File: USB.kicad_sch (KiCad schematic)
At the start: 42 parts, among them J3 USB_C_Receptacle_USB2.0, J4 USB_A_Stacked, SW4 SW_DEBUG_MODE, U2 CP2102N-Axx-xQFN24, U3 FSUSB42MUX, U4 FSUSB42MUX, U5 TPD4EUSB30, U6 USB2422, U7 AP2171W, U8 TPD4EUSB30, Y1 24MHz

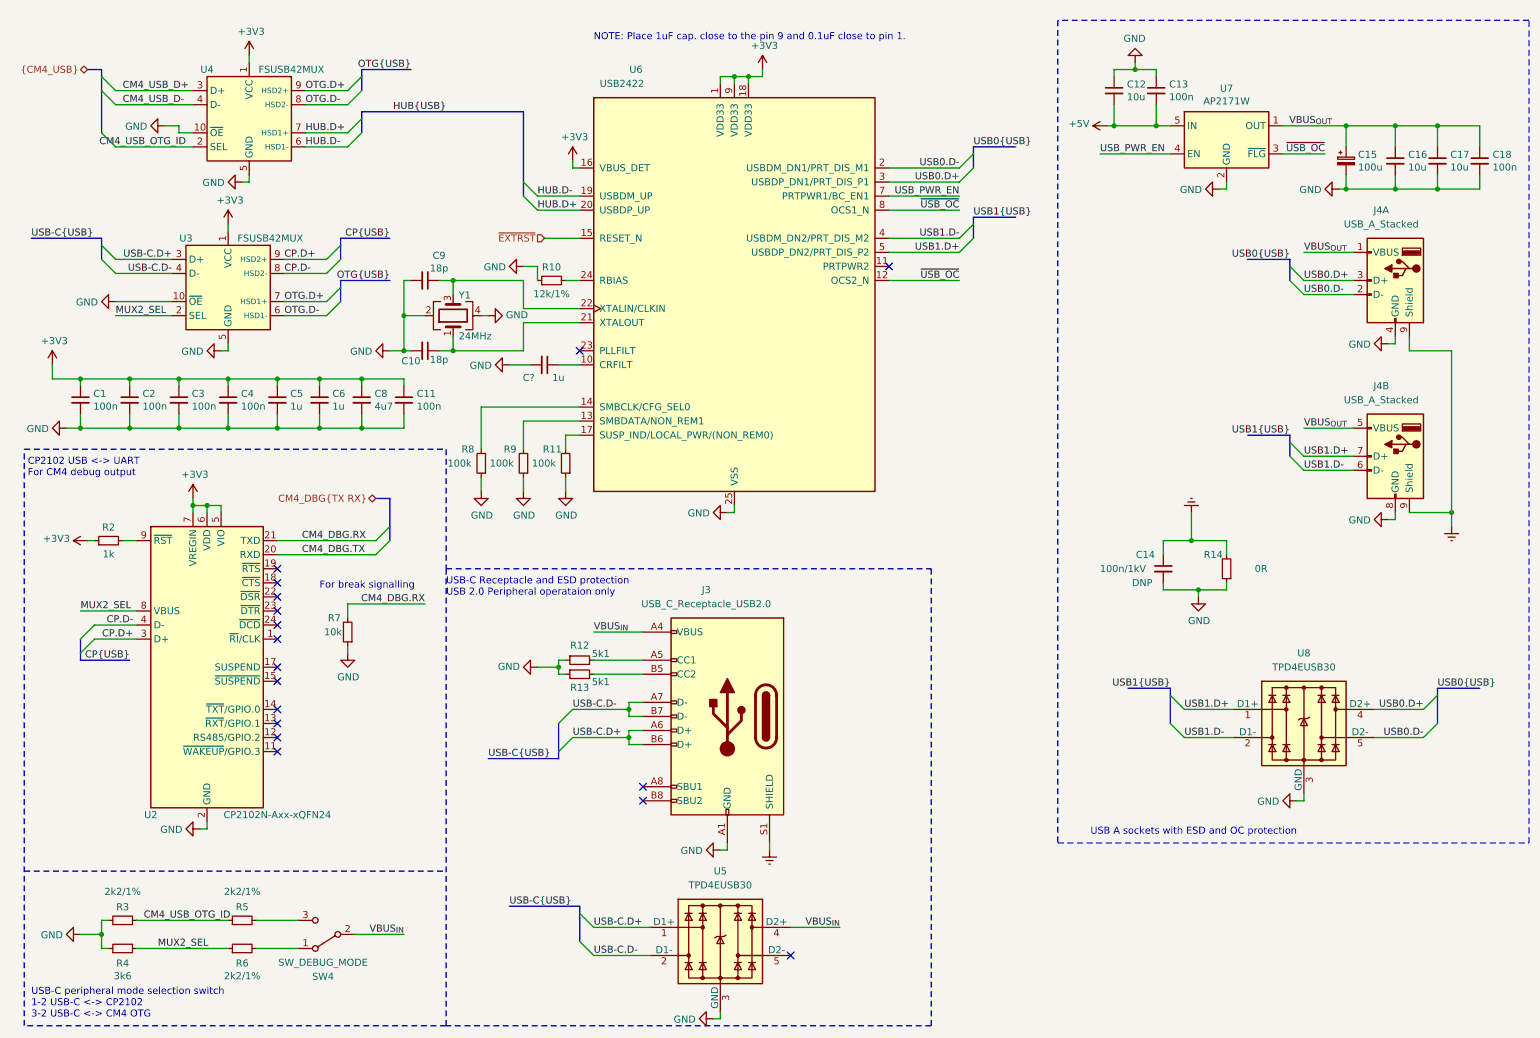
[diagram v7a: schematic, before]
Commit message: Replace CP2102N and SW4
Use a jumper instead of a switch to change between CM4 USB Device and
CP2102N. Replace CP2102N QFN24 with QFN20 variant. Make CP2102N to be
bus-powered by default.

Fixes: #7

Signed-off-by: Stefan Agner <stefan@agner.ch>
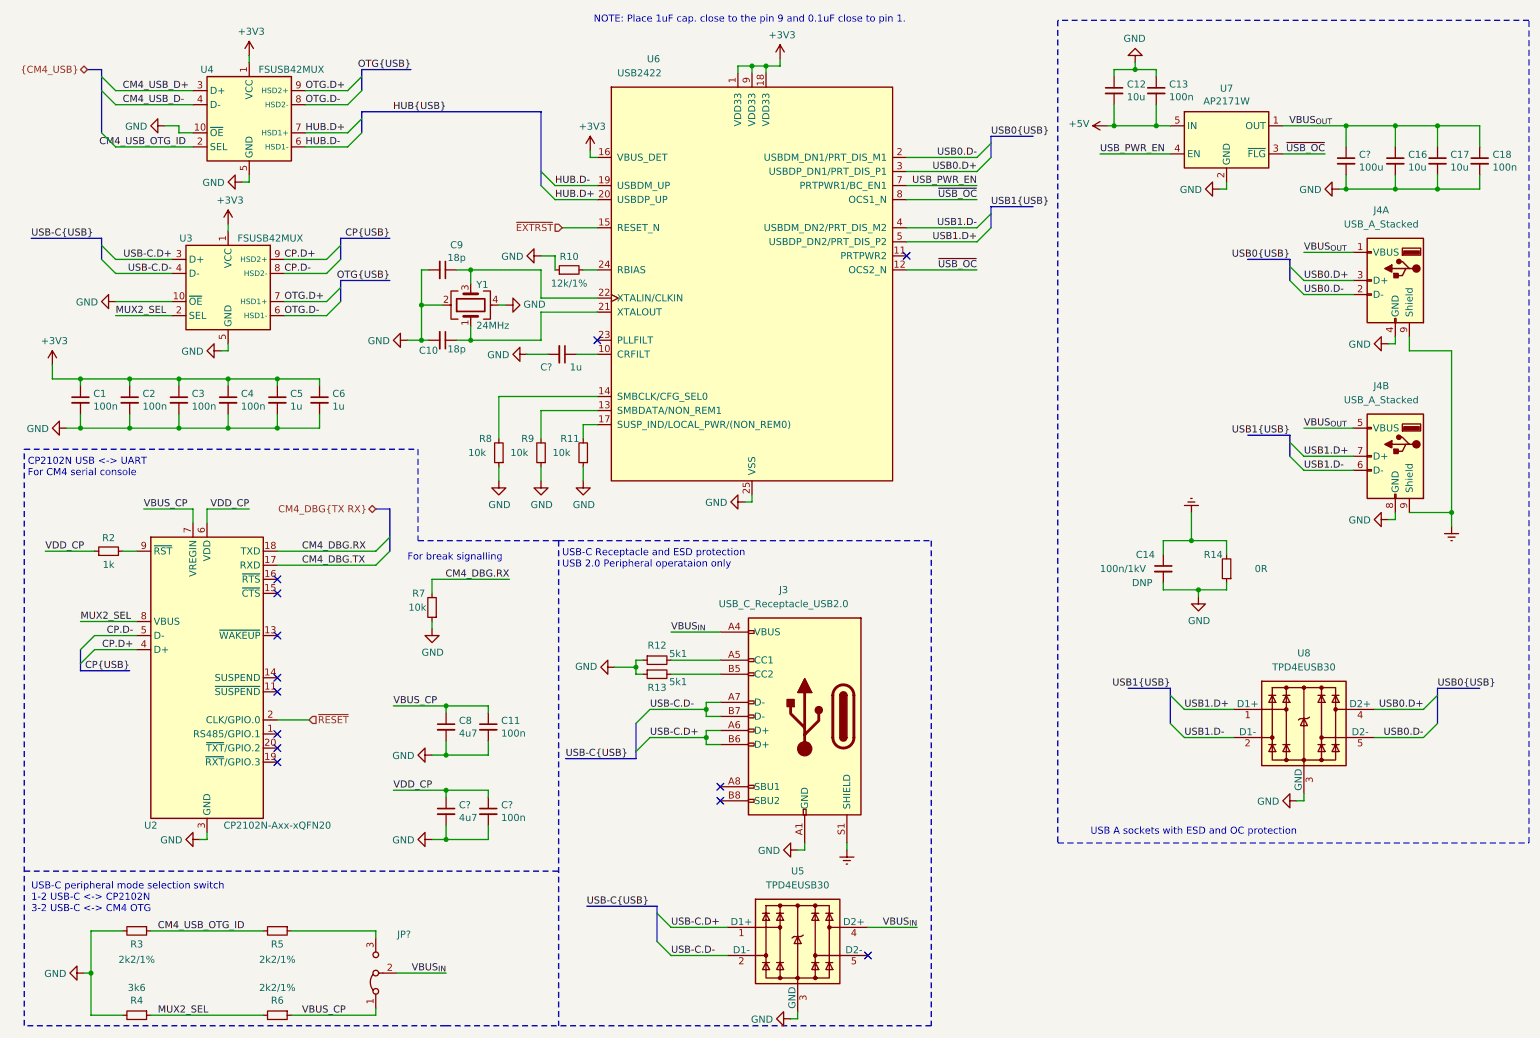
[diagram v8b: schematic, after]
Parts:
- removed C15: 100u, Capacitor_Tantalum_SMD:CP_EIA-7343-31_Kemet-D, symbol Device:CP_Small
- removed SW4: SW_DEBUG_MODE, Button_Switch_SMD:SW_SPDT_PCM12, symbol Switch:SW_SPDT
- added C?: 4u7, Capacitor_SMD:C_0402_1005Metric, symbol Device:C_Small
- added C?: 100u, Capacitor_SMD:C_0805_2012Metric, symbol Device:C_Small
- added C?: 100n, Capacitor_SMD:C_0402_1005Metric, symbol Device:C_Small
- added JP?: JP_USB_DEVICE_SEL, symbol Jumper:Jumper_3_Bridged12
- R11, R8, R9: value 100k -> 10k
- U2: value CP2102N-Axx-xQFN24 -> CP2102N-Axx-xQFN20; footprint Package_DFN_QFN:QFN-24-1EP_4x4mm_P0.5mm_EP2.6x2.6mm -> Package_DFN_QFN:SiliconLabs_QFN-20-1EP_3x3mm_P0.5mm; symbol Interface_USB:CP2102N-Axx-xQFN24 -> Interface_USB:CP2102N-Axx-xQFN20; PartNumber CP2102N-A02-GQFN24 -> CP2102N-A02-GQFN20
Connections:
- net +3V3: no longer C11.1, C8.1, R2.1, U2.5 (VIO), U2.6 (VDD), U2.7 (VREGIN)
- net CM4_DBG.RX: now also U2.18 (TXD); no longer U2.21 (TXD)
- net CM4_DBG.TX: now also U2.17 (RXD); no longer U2.20 (RXD)
- net CM4_USB_OTG_ID: now also R3.1, R5.2; no longer R3.2, R5.1
- net CP.D+: now also U2.4 (D+); no longer U2.3 (D+)
- net CP.D-: now also U2.5 (D-); no longer U2.4 (D-)
- net GND: now also R3.2, R4.2, U2.12 (GND), U2.21 (GND), U2.3 (GND), C?.2, C?.2, C?.2; no longer R3.1, R4.1, U2.2 (GND), U2.25 (GND)
- net MUX2_SEL: now also R4.1, R6.2; no longer R4.2, R6.1
- net VBUS_{IN}: now also JP?.2 (C)
- net VBUS_{OUT}: now also C?.1
- new net: JP?.3 (B), R5.1
- new net VBUS_CP: C11.1, C8.1, JP?.1 (A), R6.1, U2.7 (VREGIN)
- new net VDD_CP: C?.1, C?.1, R2.1, U2.6 (VDD)
- new net ~RESET: U2.2 (CLK/GPIO.0)
- no-connect marks 17 -> 13
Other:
- note added: "CP2102N USB <-> UART For CM4 serial console"
- note added: "USB-C peripheral mode selection switch 1-2 USB-C <-> CP2102N 3-2 USB-C <-> CM4 OTG"
- note removed: "CP2102 USB <-> UART For CM4 debug output"
- note removed: "USB-C peripheral mode selection switch 1-2 USB-C <-> CP2102 3-2 USB-C <-> CM4 OTG"
- moved on the sheet: C10, C11, C8, C9, C?, J3, R10, R11, R12, R13, R2, R3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
